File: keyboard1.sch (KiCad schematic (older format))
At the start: 46 parts, among them SW1 SW_PUSH, SW10 SW_PUSH, SW11 SW_PUSH, SW12 SW_PUSH, SW13 SW_PUSH, SW14 SW_PUSH, SW15 SW_PUSH, SW16 SW_PUSH, SW17 SW_PUSH, SW18 SW_PUSH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

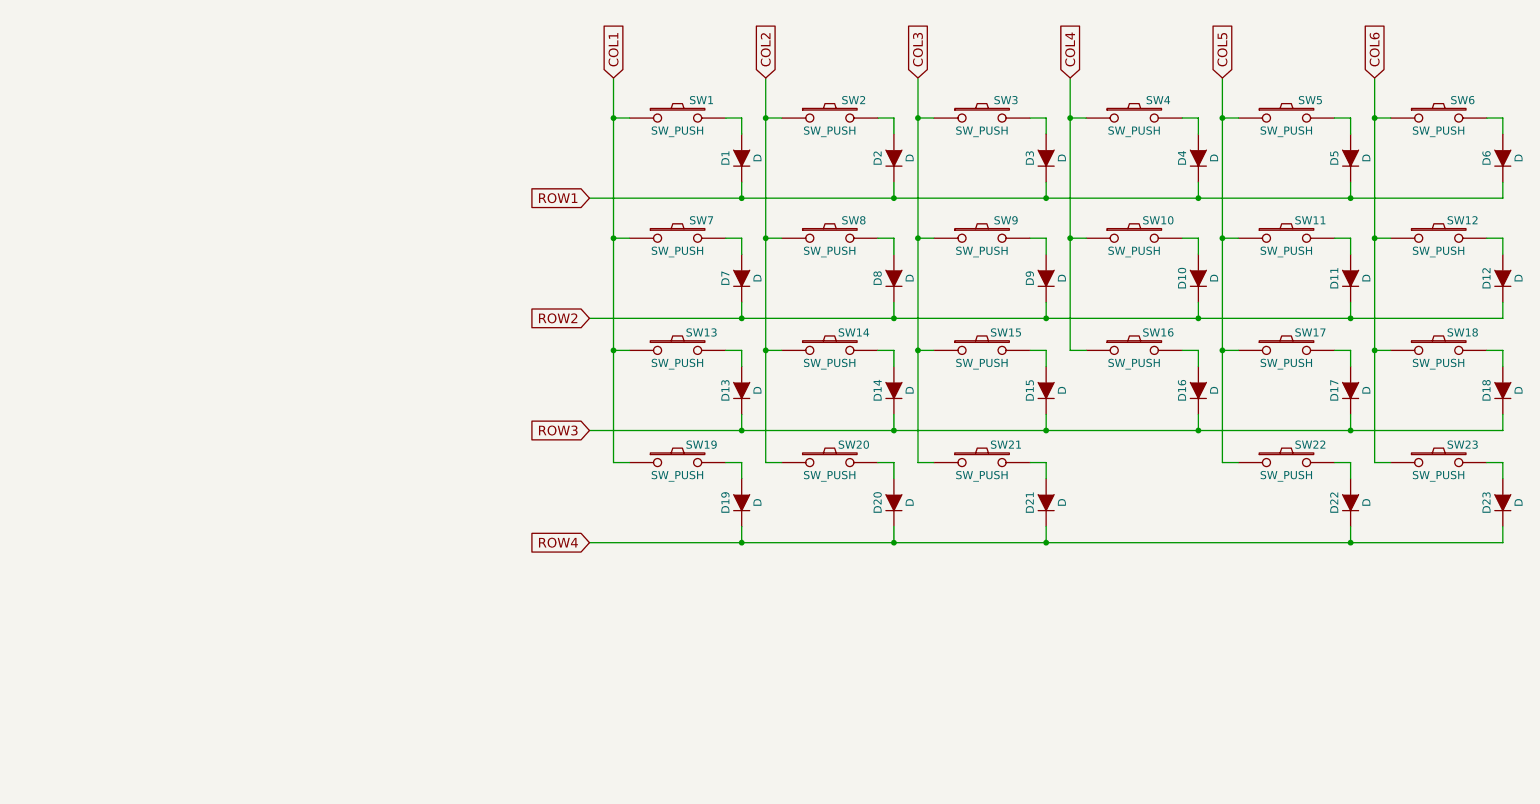
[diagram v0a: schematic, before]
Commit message: Basic schematic complete, routing in progress
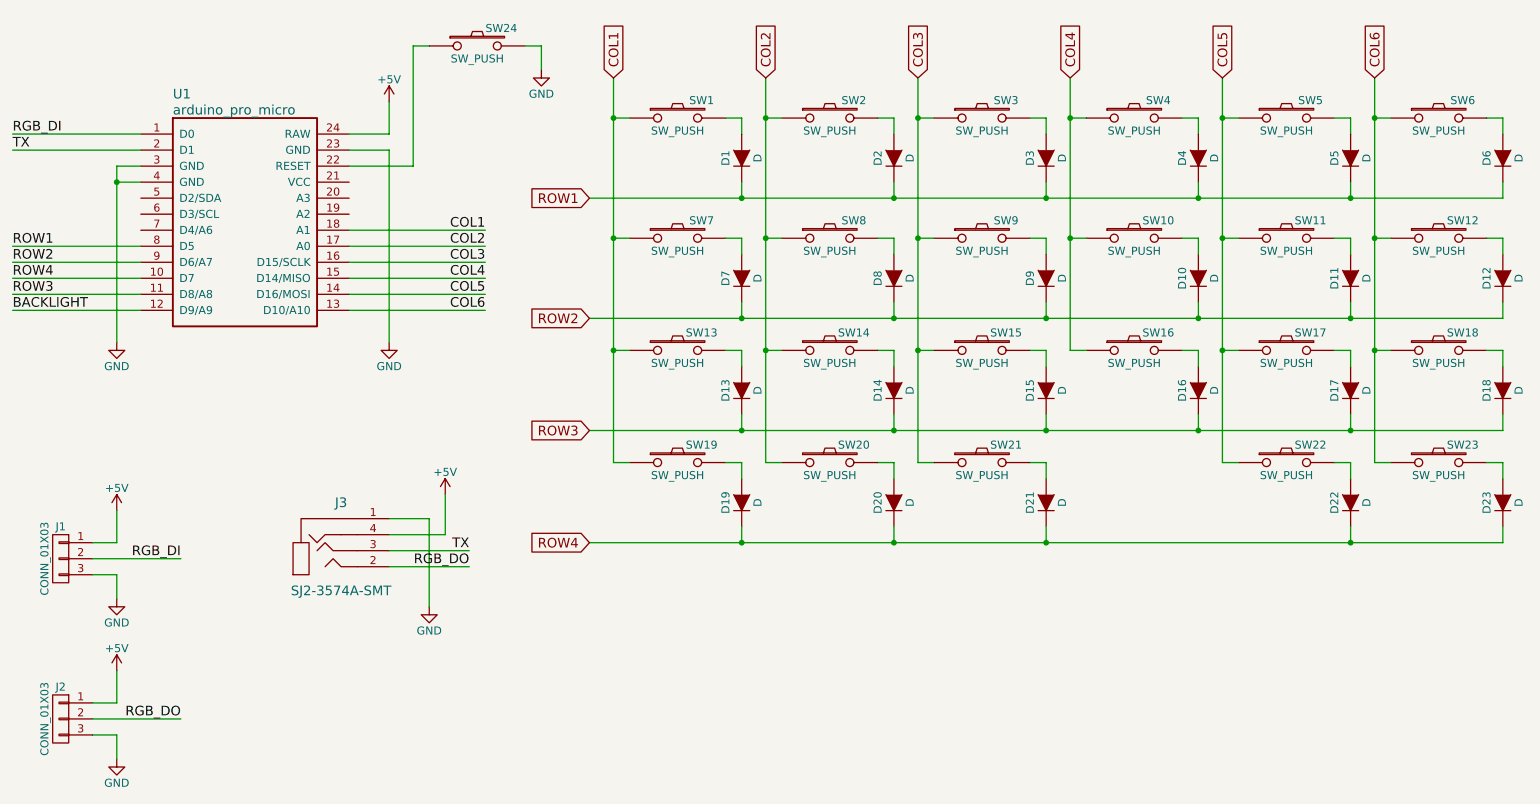
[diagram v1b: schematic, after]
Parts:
- added J1, J2: CONN_01X03, lib_fp:WS2812_3PIN, symbol CONN_01X03
- added J3: SJ2-3574A-SMT, lib_fp:SJ2-3574A-SMT, symbol SJ2-3574A-SMT
- added SW24: SW_PUSH, Buttons_Switches_SMD:SW_SPST_EVQP7C, symbol SW_PUSH
- added U1: arduino_pro_micro, lib_fp:arduino-pro-micro, symbol arduino_pro_micro
- SW1, SW10, SW11, SW12, SW13, SW14, SW15, SW16, SW17, SW18, SW2, SW3, SW4, SW5, SW6, SW7, SW8, SW9: footprint Keyboard:CHERRY_PCB_100H -> lib_fp:CHERRY_PCB_100H
- SW19, SW20, SW21, SW23: footprint Keyboard:CHERRY_PCB_125H -> lib_fp:CHERRY_PCB_125H
- SW22: footprint Keyboard:CHERRY_PCB_100H -> lib_fp:CHERRY_PCB_125H
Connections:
- net COL1: now also U1.18 (A1)
- net COL2: now also U1.17 (A0)
- net COL3: now also U1.16 (D15/SCLK)
- net COL4: now also U1.15 (D14/MISO)
- net COL5: now also U1.14 (D16/MOSI)
- net COL6: now also U1.13 (D10/A10)
- net ROW1: now also U1.8 (D5)
- net ROW2: now also U1.9 (D6/A7)
- net ROW3: now also U1.11 (D8/A8)
- net ROW4: now also U1.10 (D7)
- new net: SW24.1, U1.22 (RESET)
- new net +5V: J1.1 (P1), J2.1 (P1), J3.4, U1.24 (RAW)
- new net BACKLIGHT: U1.12 (D9/A9)
- new net GND: J1.3 (P3), J2.3 (P3), J3.1, SW24.2, U1.23 (GND), U1.3 (GND), U1.4 (GND)
- new net RGB_DI: J1.2 (P2), U1.1 (D0)
- new net RGB_DO: J2.2 (P2), J3.2
- new net TX: J3.3, U1.2 (D1)
